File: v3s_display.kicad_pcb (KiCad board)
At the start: 4 copper layers, 25.3 x 53.3 mm, 67 parts, among them J1 Conn_01x08, J2 Conn_01x08, J3 Conn_01x08, J4 Conn_01x08, Q1 Q_PMOS_GSD, U1 AXP22x

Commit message: Add tooling holes
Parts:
- added H1: MountingHole, ToolingHole:ToolingHole_JLCSMT, F.Cu at (134.6, 68.6)
- added H2: MountingHole, ToolingHole:ToolingHole_JLCSMT, F.Cu at (151.2, 116.7)
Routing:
- net /DC1SW: track 30.1 -> 33.7 mm
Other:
- board text added: "AXP22x breakout Rev A Designed by Tobias Schramm 2021"
- board text added: "JLCJLCJLCJLC"

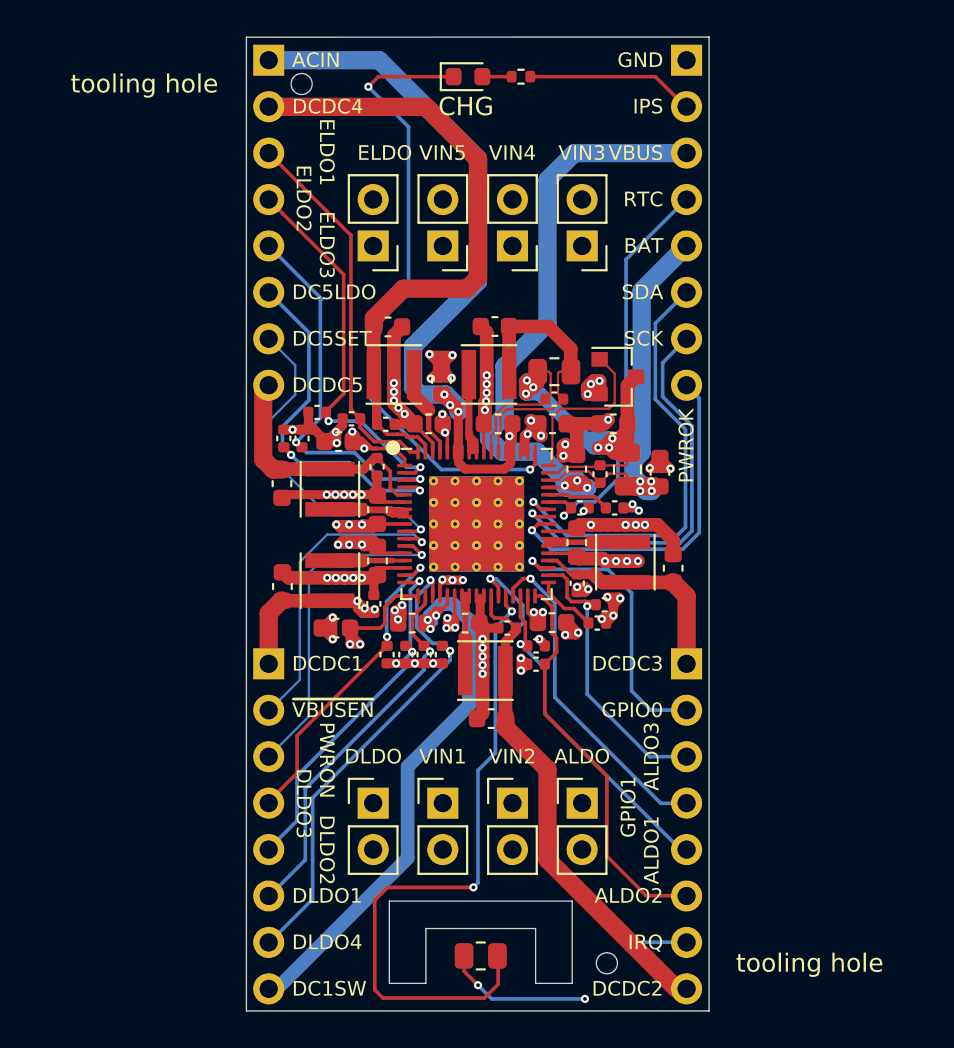
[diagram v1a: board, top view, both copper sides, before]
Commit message: Improve power routing a little
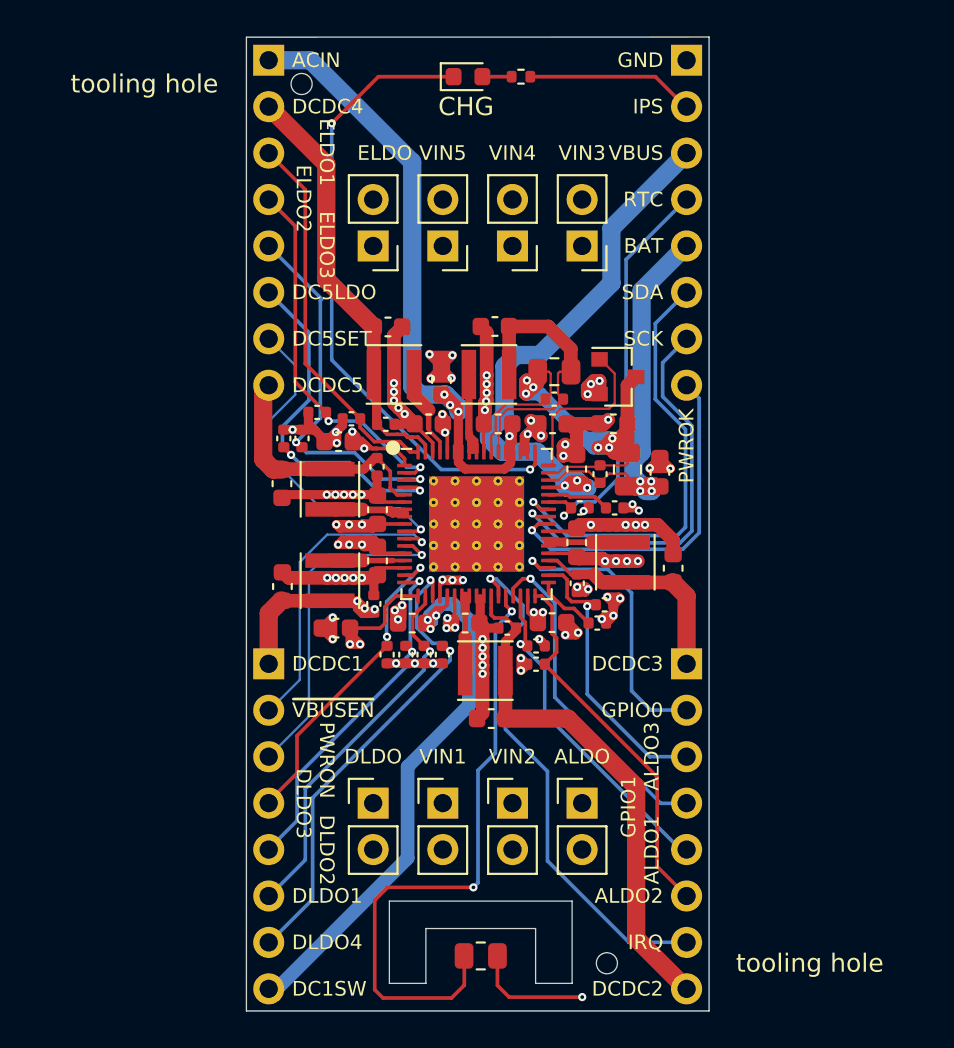
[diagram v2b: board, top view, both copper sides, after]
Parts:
- turned TH1 to 0 degrees
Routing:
- net /DCDC4: track 34.6 -> 22.8 mm
- net +5V: track 48.4 -> 43.2 mm
- net /VBUS_: track 37.5 -> 34.7 mm
- net Net-(TH1-Pad1): track 36.3 -> 34.5 mm
- net /DCDC2: track 27.1 -> 28.7 mm
- net GND: track 99.0 -> 97.4 mm, vias 65 -> 64
- net /ALDO2: track 22.0 -> 20.7 mm
- net /ELDO2: track 21.3 -> 20.6 mm
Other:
- board text added: "AXP22x breakout Rev B Designed by Tobias Schramm 2021"
- board text removed: "AXP22x breakout Rev A Designed by Tobias Schramm 2021"

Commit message: Increase trace width on LDOs
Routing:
- net /ALDO2: track 20.7 -> 36.6 mm
- net /DLDO3: track 17.4 -> 23.9 mm, vias 2 -> 3
- net /DCDC1: track 31.5 -> 36.3 mm
- net /CHGLED: track 35.1 -> 33.2 mm
- net /DLDO4: track 26.8 -> 28.4 mm, vias 2 -> 3
- net /DLDO2: track 19.5 -> 20.9 mm, vias 2 -> 3
- net /ELDO2: track 20.6 -> 21.7 mm, vias 2 -> 3
- net /DLDO1: track 20.8 -> 21.9 mm, vias 1 -> 2
- net /ALDO3: track 15.9 -> 16.6 mm, vias 1 -> 2
